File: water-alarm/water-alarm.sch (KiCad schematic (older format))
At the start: 51 parts, among them M1 Motor_Servo, M2 Motor_Servo, Q1 BC327, Q2 BC327, Q3 BC327, Q4 BC327, SW1 SW_Push, SW2 SW_Push, U1 Arduino_Pro_Mini, U2 AMS1117-3.3

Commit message: Update water-alarm.sch
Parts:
- added R? (x2): 10K, symbol Device:R
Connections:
- net SERVO1_FEEDBACK: now also R?.2; no longer C8.2, M1.3 (-), R17.1
- net SERVO2_FEEDBACK: now also R?.2; no longer C9.2, M2.3 (-), R18.1
- new net: C8.2, M1.3 (-), R17.1, R?.1
- new net: C9.2, M2.3 (-), R18.1, R?.1
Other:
- moved on the sheet: C6, C7
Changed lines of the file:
@@
 SERVO1_FEEDBACK
 Wire Wire Line
-	8700 1950 8950 1950
+	8700 1950 8800 1950
 $Comp
 L Device:C C6
 U 1 1 5DBC069B
-P 8950 2150
-F 0 "C6" H 9065 2196 50  0000 L CNN
-F 1 "100nF" H 9065 2105 50  0000 L CNN
-F 2 "" H 8988 2000 50  0001 C CNN
-F 3 "~" H 8950 2150 50  0001 C CNN
-	1    8950 2150
-	1    0    0    -1
-$EndComp
-Wire Wire Line
-	8950 2000 8950 1950
-Connection ~ 8950 1950
-Wire Wire Line
-	8950 1950 9400 1950
-Wire Wire Line
-	8950 2300 8950 2350
-Wire Wire Line
-	8950 2350 9400 2350
+P 8800 2150
+F 0 "C6" H 8915 2196 50  0000 L CNN
+F 1 "100nF" H 8915 2105 50  0000 L CNN
+F 2 "" H 8838 2000 50  0001 C CNN
+F 3 "~" H 8800 2150 50  0001 C CNN
+	1    8800 2150
+	1    0    0    -1
+$EndComp
+Wire Wire Line
+	8800 2000 8800 1950
+Wire Wire Line
+	8800 2300 8800 2350
+Wire Wire Line
+	8800 2350 9400 2350
 Wire Wire Line
 	9400 2350 9400 2400
@@
 SERVO2_FEEDBACK
 Wire Wire Line
-	8700 3900 8950 3900
+	8700 3900 8800 3900
 $Comp
 L Device:C C7
 U 1 1 5DBC81A7
-P 8950 4100
-F 0 "C7" H 9065 4146 50  0000 L CNN
-F 1 "100nF" H 9065 4055 50  0000 L CNN
-F 2 "" H 8988 3950 50  0001 C CNN
-F 3 "~" H 8950 4100 50  0001 C CNN
-	1    8950 4100
-	1    0    0    -1
-$EndComp
-Wire Wire Line
-	8950 3950 8950 3900
-Connection ~ 8950 3900
-Wire Wire Line
-	8950 3900 9400 3900
-Wire Wire Line
-	8950 4250 8950 4300
-Wire Wire Line
-	8950 4300 9400 4300
+P 8800 4100
+F 0 "C7" H 8915 4146 50  0000 L CNN
+F 1 "100nF" H 8915 4055 50  0000 L CNN
+F 2 "" H 8838 3950 50  0001 C CNN
+F 3 "~" H 8800 4100 50  0001 C CNN
+	1    8800 4100
+	1    0    0    -1
+$EndComp
+Wire Wire Line
+	8800 3950 8800 3900
+Wire Wire Line
+	8800 4250 8800 4300
+Wire Wire Line
+	8800 4300 9400 4300
 Wire Wire Line
 	9400 4300 9400 4350
@@
 Wire Wire Line
 	5100 5750 5400 5750
+$Comp
+L Device:R R?
+U 1 1 5DE7D4D4
+P 9100 3900
+F 0 "R?" V 8893 3900 50  0000 C CNN
+F 1 "10K" V 8984 3900 50  0000 C CNN
+F 2 "" V 9030 3900 50  0001 C CNN
+F 3 "~" H 9100 3900 50  0001 C CNN
+	1    9100 3900
+	0    1    1    0
+$EndComp
+Wire Wire Line
+	9250 3900 9400 3900
+Wire Wire Line
+	8800 3900 8950 3900
+Connection ~ 8800 3900
+$Comp
+L Device:R R?
+U 1 1 5DEB3C68
+P 9100 1950
+F 0 "R?" V 8893 1950 50  0000 C CNN
+F 1 "10K" V 8984 1950 50  0000 C CNN
+F 2 "" V 9030 1950 50  0001 C CNN
+F 3 "~" H 9100 1950 50  0001 C CNN
+	1    9100 1950
+	0    1    1    0
+$EndComp
+Wire Wire Line
+	9250 1950 9400 1950
+Wire Wire Line
+	8950 1950 8800 1950
+Connection ~ 8800 1950
 $EndSCHEMATC

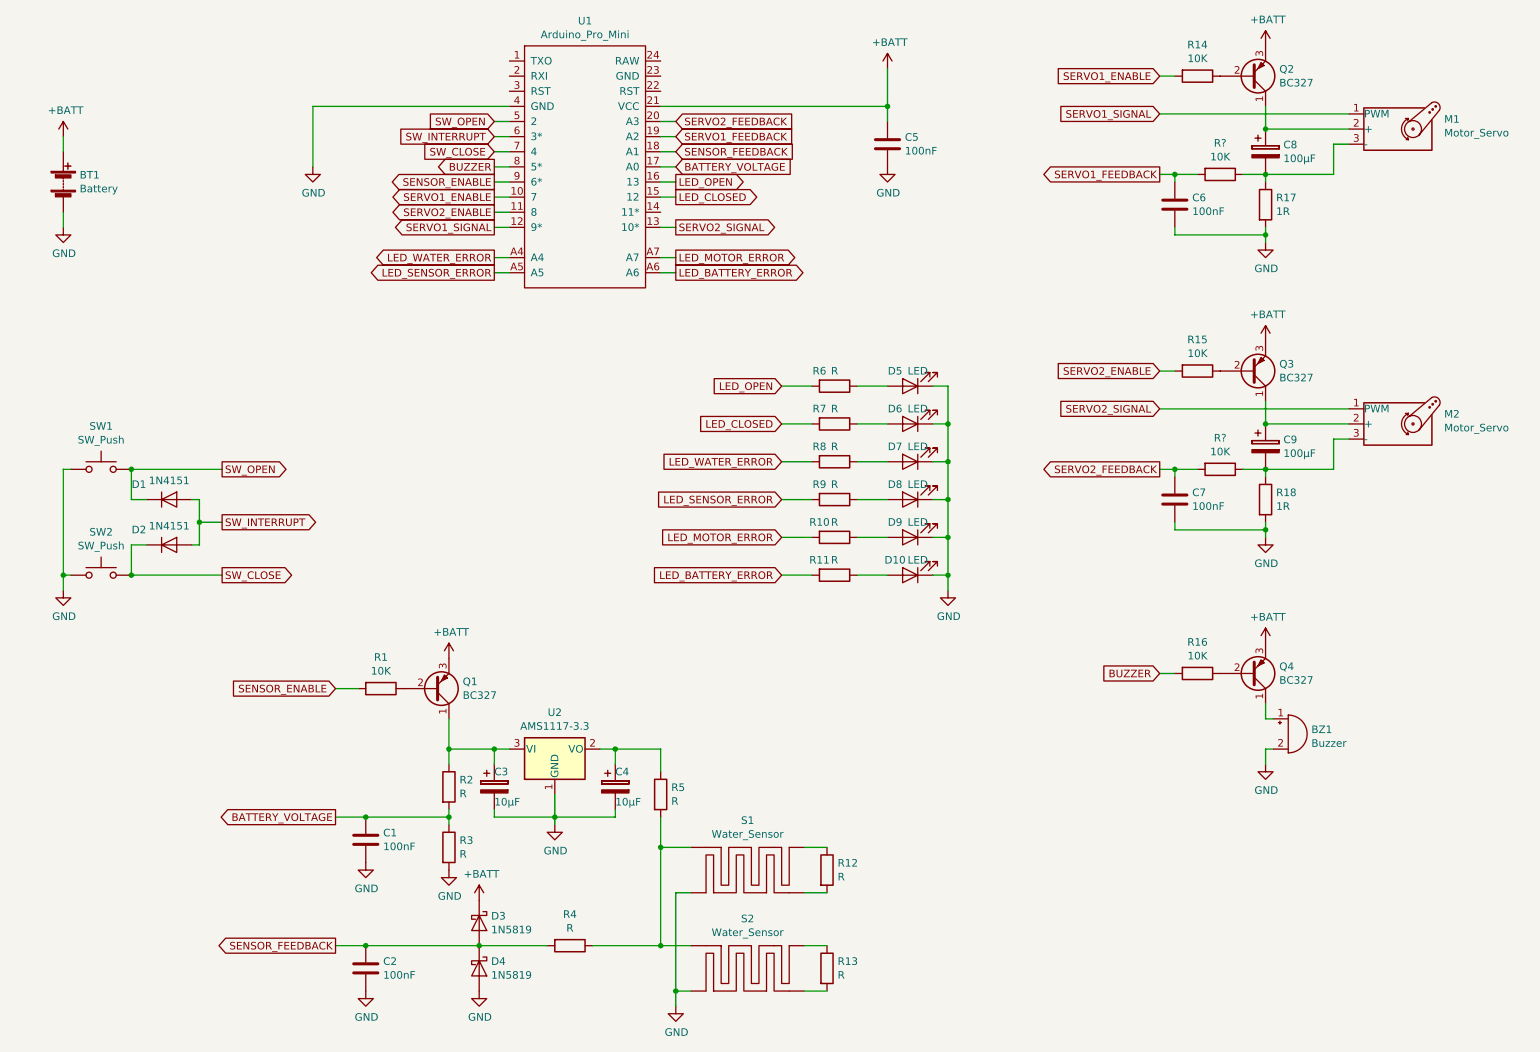
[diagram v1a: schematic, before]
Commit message: Update water-alarm.sch
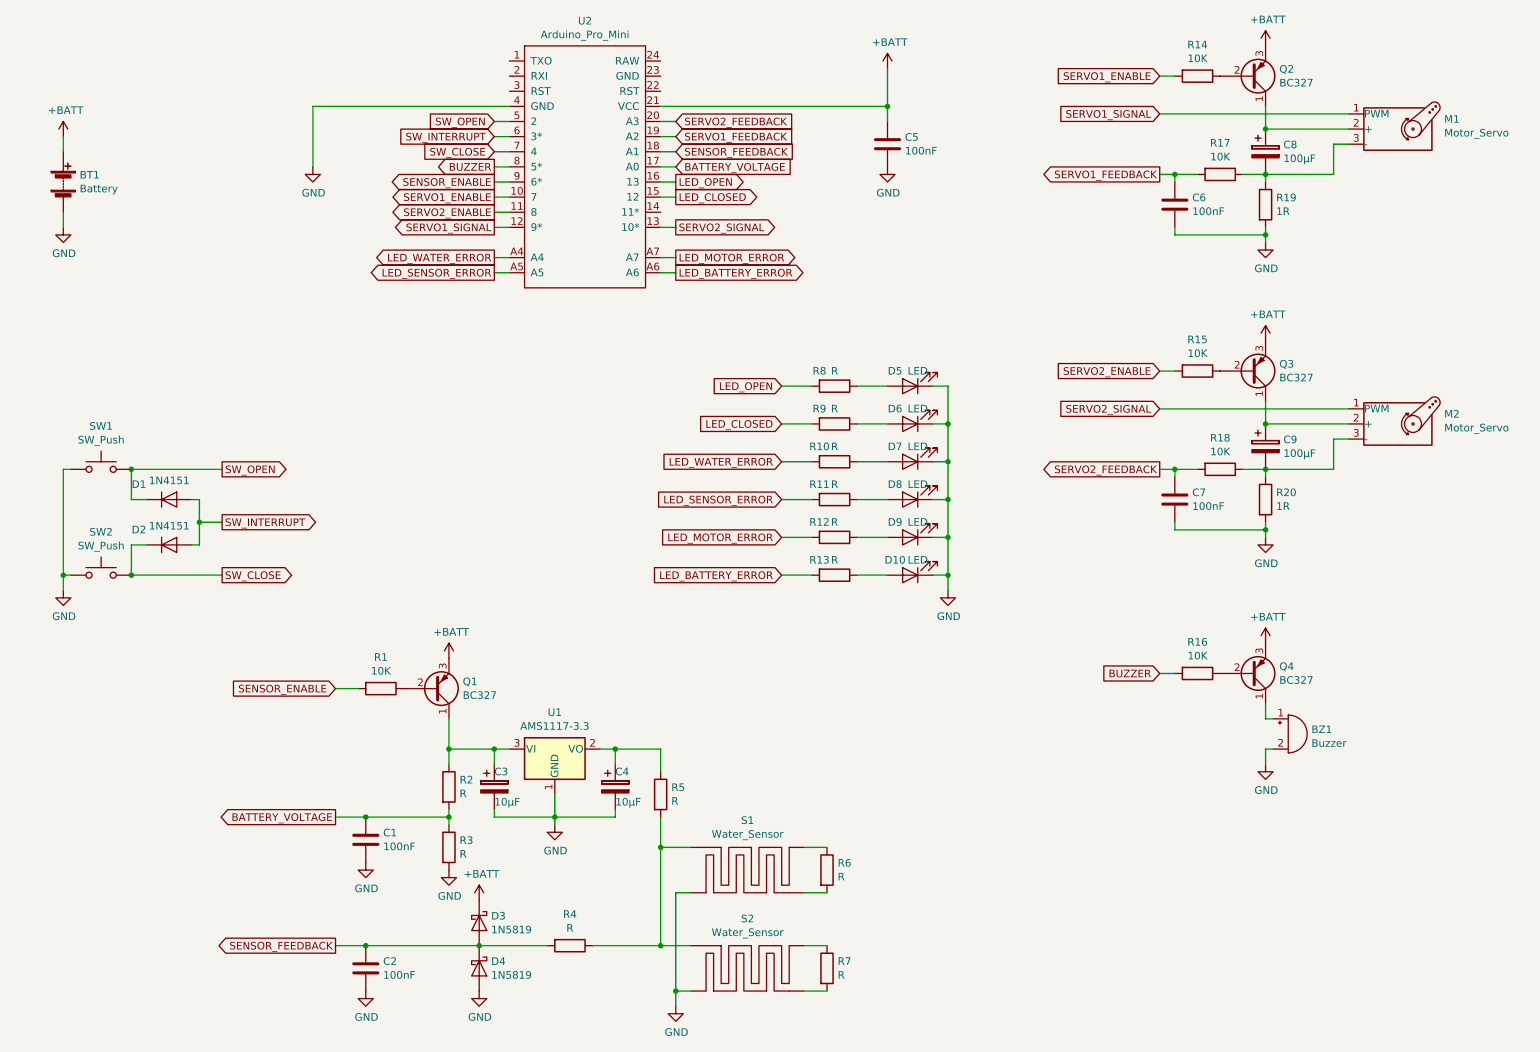
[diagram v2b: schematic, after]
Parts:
- gave numbers to parts that had none: 2
- renumbered R8 to R10, R9 to R11, R10 to R12, R11 to R13, R17 to R19, R18 to R20, R12 to R6, R13 to R7, R6 to R8, R7 to R9, U2 to U1, U1 to U2
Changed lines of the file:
@@
 $EndDescr
 $Comp
-L microfarad-de:Arduino_Pro_Mini U1
+L microfarad-de:Arduino_Pro_Mini U2
 U 1 1 5DB8710D
 P 4900 1900
-F 0 "U1" H 4900 2865 50  0000 C CNN
+F 0 "U2" H 4900 2865 50  0000 C CNN
 F 1 "Arduino_Pro_Mini" H 4900 2774 50  0000 C CNN
 F 2 "" H 5000 2300 50  0001 C CNN
@@
 $EndComp
 $Comp
-L Device:R R6
+L Device:R R8
 U 1 1 5DB87461
 P 6550 3350
-F 0 "R6" V 6450 3250 50  0000 C CNN
+F 0 "R8" V 6450 3250 50  0000 C CNN
 F 1 "R" V 6450 3350 50  0000 C CNN
 F 2 "" V 6480 3350 50  0001 C CNN
@@
 $EndComp
 $Comp
-L Regulator_Linear:AMS1117-3.3 U2
+L Regulator_Linear:AMS1117-3.3 U1
 U 1 1 5DB876FC
 P 4700 5750
-F 0 "U2" H 4700 5992 50  0000 C CNN
+F 0 "U1" H 4700 5992 50  0000 C CNN
 F 1 "AMS1117-3.3" H 4700 5901 50  0000 C CNN
 F 2 "Package_TO_SOT_SMD:SOT-223-3_TabPin2" H 4700 5950 50  0001 C CNN
@@
 $EndComp
 $Comp
-L Device:R R12
+L Device:R R6
 U 1 1 5DB890D2
 P 6500 6550
-F 0 "R12" H 6570 6596 50  0000 L CNN
+F 0 "R6" H 6570 6596 50  0000 L CNN
 F 1 "R" H 6570 6505 50  0000 L CNN
 F 2 "" V 6430 6550 50  0001 C CNN
@@
 $EndComp
 $Comp
-L Device:R R13
+L Device:R R7
 U 1 1 5DB89136
 P 6500 7200
-F 0 "R13" H 6570 7246 50  0000 L CNN
+F 0 "R7" H 6570 7246 50  0000 L CNN
 F 1 "R" H 6570 7155 50  0000 L CNN
 F 2 "" V 6430 7200 50  0001 C CNN
@@
 	9400 5750 9450 5750
 $Comp
-L Device:R R17
+L Device:R R19
 U 1 1 5DBBC316
 P 9400 2150
-F 0 "R17" H 9470 2196 50  0000 L CNN
+F 0 "R19" H 9470 2196 50  0000 L CNN
 F 1 "1R" H 9470 2105 50  0000 L CNN
 F 2 "" V 9330 2150 50  0001 C CNN
@@
 	8700 3250 8800 3250
 $Comp
-L Device:R R18
+L Device:R R20
 U 1 1 5DBC819D
 P 9400 4100
-F 0 "R18" H 9470 4146 50  0000 L CNN
+F 0 "R20" H 9470 4146 50  0000 L CNN
 F 1 "1R" H 9470 4055 50  0000 L CNN
 F 2 "" V 9330 4100 50  0001 C CNN
@@
 $EndComp
 $Comp
-L Device:R R7
+L Device:R R9
 U 1 1 5DC11EBD
 P 6550 3600
-F 0 "R7" V 6450 3500 50  0000 C CNN
+F 0 "R9" V 6450 3500 50  0000 C CNN
 F 1 "R" V 6450 3600 50  0000 C CNN
 F 2 "" V 6480 3600 50  0001 C CNN
@@
 $EndComp
 $Comp
-L Device:R R8
+L Device:R R10
 U 1 1 5DC11F1A
 P 6550 3850
-F 0 "R8" V 6450 3750 50  0000 C CNN
+F 0 "R10" V 6450 3750 50  0000 C CNN
 F 1 "R" V 6450 3850 50  0000 C CNN
 F 2 "" V 6480 3850 50  0001 C CNN
@@
 $EndComp
 $Comp
-L Device:R R9
+L Device:R R11
 U 1 1 5DC11F7B
 P 6550 4100
-F 0 "R9" V 6450 4000 50  0000 C CNN
+F 0 "R11" V 6450 4000 50  0000 C CNN
 F 1 "R" V 6450 4100 50  0000 C CNN
 F 2 "" V 6480 4100 50  0001 C CNN
@@
 $EndComp
 $Comp
-L Device:R R10
+L Device:R R12
 U 1 1 5DC11FDE
 P 6550 4350
-F 0 "R10" V 6450 4250 50  0000 C CNN
+F 0 "R12" V 6450 4250 50  0000 C CNN
 F 1 "R" V 6450 4350 50  0000 C CNN
 F 2 "" V 6480 4350 50  0001 C CNN
@@
 $EndComp
 $Comp
-L Device:R R11
+L Device:R R13
 U 1 1 5DC12042
 P 6550 4600
-F 0 "R11" V 6450 4500 50  0000 C CNN
+F 0 "R13" V 6450 4500 50  0000 C CNN
 F 1 "R" V 6450 4600 50  0000 C CNN
 F 2 "" V 6480 4600 50  0001 C CNN
@@
 	5100 5750 5400 5750
 $Comp
-L Device:R R?
+L Device:R R18
 U 1 1 5DE7D4D4
 P 9100 3900
-F 0 "R?" V 8893 3900 50  0000 C CNN
+F 0 "R18" V 8893 3900 50  0000 C CNN
 F 1 "10K" V 8984 3900 50  0000 C CNN
 F 2 "" V 9030 3900 50  0001 C CNN
@@
 Connection ~ 8800 3900
 $Comp
-L Device:R R?
+L Device:R R17
 U 1 1 5DEB3C68
 P 9100 1950
-F 0 "R?" V 8893 1950 50  0000 C CNN
+F 0 "R17" V 8893 1950 50  0000 C CNN
 F 1 "10K" V 8984 1950 50  0000 C CNN
 F 2 "" V 9030 1950 50  0001 C CNN

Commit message: Update water-alarm.sch
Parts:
- removed C8, C9: 100µF, symbol Device:CP
- added C?: 470µF, symbol Device:CP
- BT1: value Battery -> 4 x 1.5V
- M1, M2: value Motor_Servo -> 360° Servo
- R2: value R -> 4K7
- R3: value R -> 1K
- R4: value R -> 10K
- S1, S2: value Water_Sensor -> Water Sensor
- U2: value Arduino_Pro_Mini -> Arduino Pro Mini
- renumbered R12 to R10, R13 to R11, R6 to R12, R7 to R13, R8 to R6, R9 to R7, R10 to R8, R11 to R9
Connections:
- net +BATT: now also C?.1
- net GND: now also C?.2
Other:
- note added: "Water Sensor System"
- moved on the sheet: BT1, C1, C2, C3, C4, C5, C6, C7, D1, D2, D3, D4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
